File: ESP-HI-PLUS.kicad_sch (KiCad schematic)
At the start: 81 parts, among them J1 USB_C_Receptacle_USB2.0_14P, J2 0.71" LCD, J3 PR5L4015-5P-C-F, J4 PR5L4015-5P-C-F, Q1 AO3401A, Q2 NTK3139P, SW1 SKRPACE010, SW2 SKRPACE010, SW3 JS102011SAQN, U1 MAX40200AUK, U2 ESP32-S3-WROOM-1, U3 TLV75733PDBV, U4 TP4065, U5 DMM-4026-B-I2S-R, U6 MAX40200AUK, U7 MAX98357A, U8 LSM6DSV16X

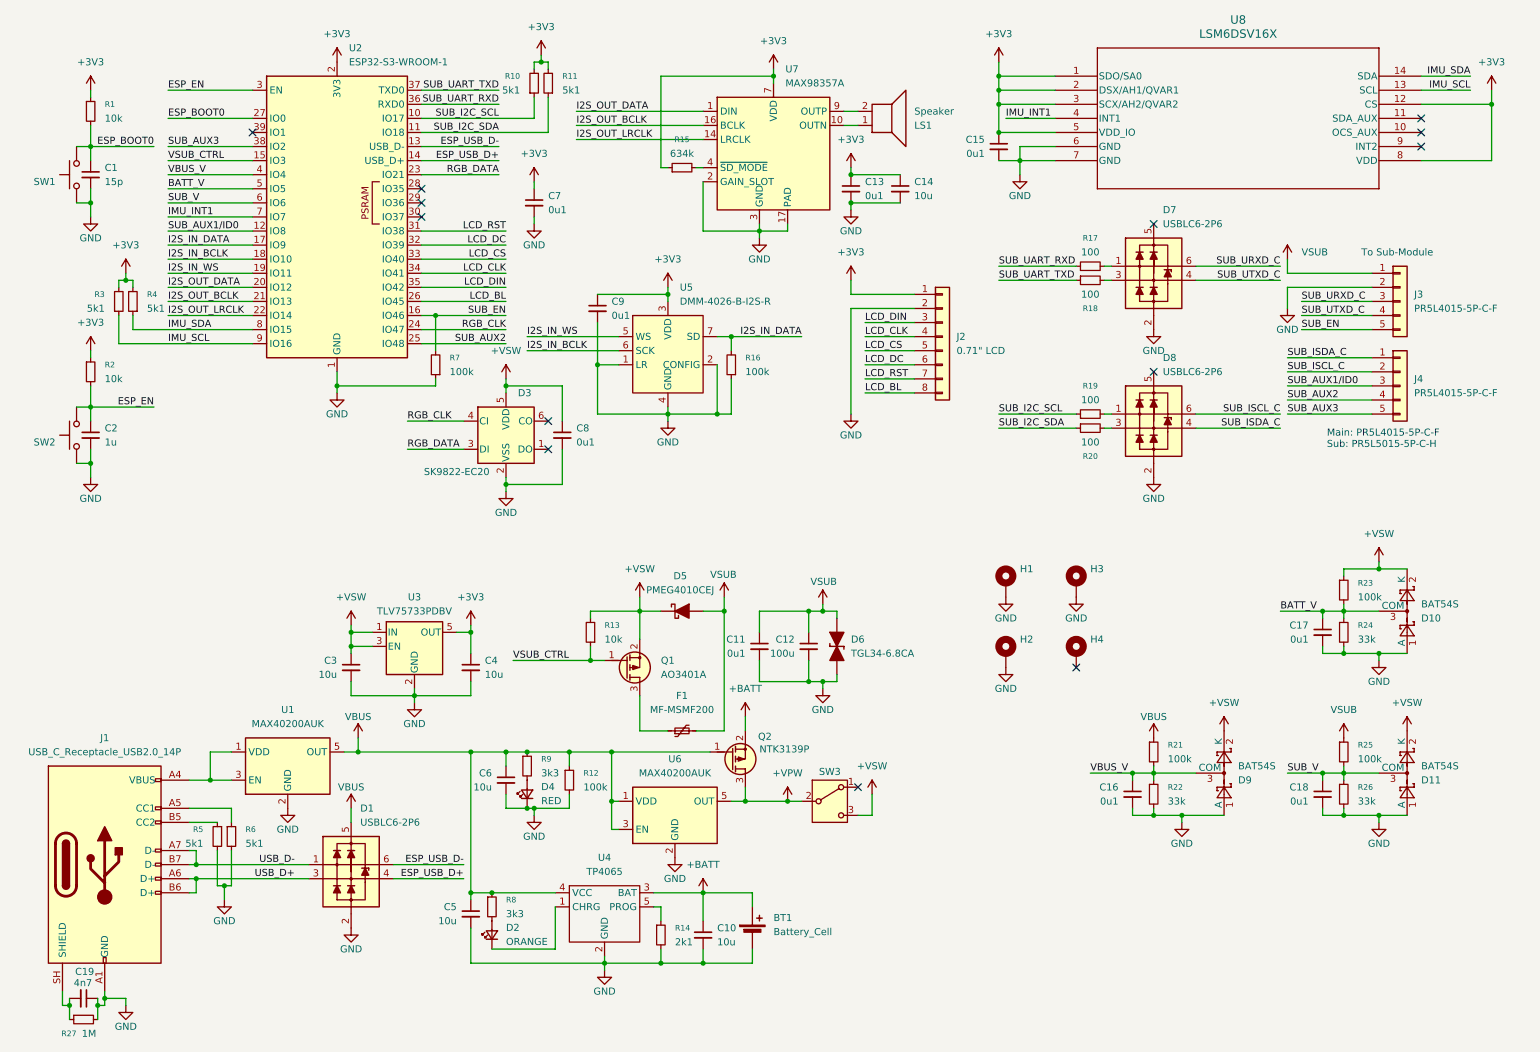
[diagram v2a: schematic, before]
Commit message: Added Sub-module Configuration Resistor and Resistor Table
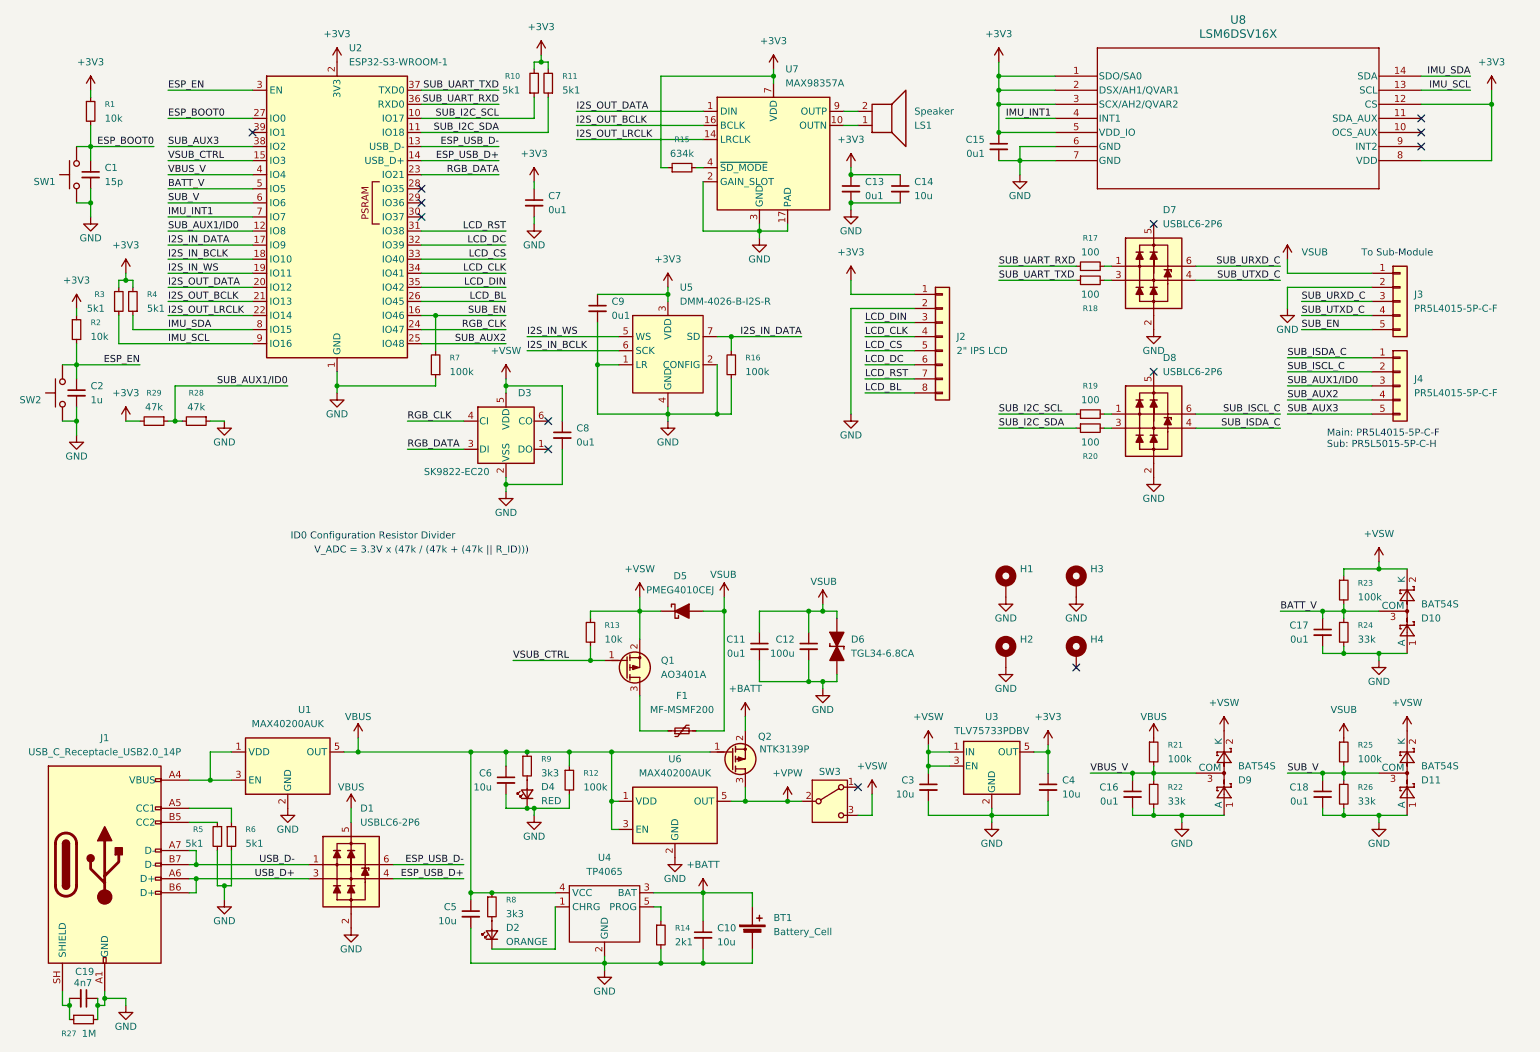
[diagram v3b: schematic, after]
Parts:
- added R28, R29: 47k, PCM_Resistor_SMD_AKL:R_0402_1005Metric, symbol Device:R_Small
- BT1, LS1: KiLib_Generator (none) -> connector/Molex
- C1, C10, C11, C12, C13, C14, C15, C16, C17, C18, C19, C2, C3, C4, C5, C6, C7, C8, C9, D2, F1: KiLib_Generator (none) -> SMD_2terminal_chip_molded
- D10, U6: KiLib_Generator (none) -> package/gullwing
- D11: footprint PCM_SparkFun-LED:APA102_2020-6Pin -> Package_TO_SOT_SMD:SOT-23; KiLib_Generator (none) -> package/gullwing
- D3: footprint LED_SMD:LED_0603_1608Metric -> PCM_SparkFun-LED:APA102_2020-6Pin
- D4: footprint PCM_Diode_SMD_AKL:D_SOD-323F -> LED_SMD:LED_0603_1608Metric; KiLib_Generator (none) -> SMD_2terminal_chip_molded
- D5: footprint Package_TO_SOT_SMD:SOT-23 -> PCM_Diode_SMD_AKL:D_SOD-323F
- D6: footprint PCM_Diode_SMD_AKL:D_SMA_TVS -> PCM_Diode_SMD_AKL:D_MiniMELF_TVS
- D7: footprint Package_TO_SOT_SMD:SOT-23 -> PCM_Package_TO_SOT_SMD_AKL:SOT-666
- D9: footprint PCM_Package_TO_SOT_SMD_AKL:SOT-666 -> Package_TO_SOT_SMD:SOT-23; KiLib_Generator (none) -> package/gullwing
- J1: footprint Connector_PinSocket_2.54mm:PinSocket_1x08_P2.54mm_Vertical -> Connector_USB:USB_C_Receptacle_HCTL_HC-TYPE-C-16P-01A
- J2: value 0.71" LCD -> 2" IPS LCD; footprint Connector_USB:USB_C_Receptacle_HCTL_HC-TYPE-C-16P-01A -> Connector_PinSocket_2.54mm:PinSocket_1x08_P2.54mm_Vertical; KiLib_Generator (none) -> connector/pin_header_socket
- J3, J4: KiLib_Generator (none) -> connector/pin_header_socket
- Q1: footprint PCM_Package_TO_SOT_SMD_AKL:SOT-723 -> PCM_Package_TO_SOT_SMD_AKL:SOT-23
- Q2: footprint PCM_Package_TO_SOT_SMD_AKL:SOT-23 -> PCM_Package_TO_SOT_SMD_AKL:SOT-723
- SW1: footprint Button_Switch_SMD:SW_SPDT_CK_JS102011SAQN -> Button_Switch_SMD:SW_Push_1P1T_NO_Vertical_Wuerth_434133025816
- SW3: footprint Button_Switch_SMD:SW_Push_1P1T_NO_Vertical_Wuerth_434133025816 -> Button_Switch_SMD:SW_SPDT_CK_JS102011SAQN
- U1: footprint RF_Module:ESP32-S3-WROOM-1 -> Package_TO_SOT_SMD:SOT-23-5; KiLib_Generator (none) -> package/gullwing
- U2: footprint MIC_DMM-4026-B-I2S-R:MIC_DMM-4026-B-I2S-R -> RF_Module:ESP32-S3-WROOM-1
- U3: footprint Package_DFN_QFN:TQFN-16-1EP_3x3mm_P0.5mm_EP1.23x1.23mm -> Package_TO_SOT_SMD:SOT-23-5; KiLib_Generator (none) -> package/gullwing
- U4: footprint LSM6DSV16X:LGA14_LSM6_STM -> PCM_Package_TO_SOT_SMD_AKL:SOT-23-5_BigPads
- U5: footprint Package_TO_SOT_SMD:SOT-23-5 -> MIC_DMM-4026-B-I2S-R:MIC_DMM-4026-B-I2S-R
- U7: footprint PCM_Package_TO_SOT_SMD_AKL:SOT-23-5_BigPads -> Package_DFN_QFN:TQFN-16-1EP_3x3mm_P0.5mm_EP1.23x1.23mm; KiLib_Generator (none) -> package/no_lead
- U8: footprint Package_TO_SOT_SMD:SOT-23-5 -> LSM6DSV16X:LGA14_LSM6_STM
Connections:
- net +3V3: now also R29.2
- net GND: now also R28.1
- net SUB_AUX1/ID0: now also R28.2, R29.1
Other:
- note added: "ID0 Configuration Resistor Divider"
- note added: "V_ADC = 3.3V x (47k / (47k + (47k || R_ID)))"
- title: (none) -> ESP-HI-PLUS
- moved on the sheet: C2, C3, C4, R2, SW2, U3

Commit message: ESP-HI-PLUS v1.1: added microSD card slot and combined I2S in/out ports
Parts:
- added J5: Micro_SD_Card, Connector_Card:microSD_HC_Hirose_DM3AT-SF-PEJM5, symbol Connector:Micro_SD_Card
- added R30, R31, R32, R33: 10k, PCM_Resistor_SMD_AKL:R_0402_1005Metric, symbol Device:R_Small
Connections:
- net +3V3: now also J5.4 (VDD), R30.2, R31.2, R32.2, R33.2
- net GND: now also J5.6 (VSS)
- net I2S_IN_BCLK: now also U7.16 (BCLK)
- net I2S_IN_DATA: now also U7.1 (DIN)
- net I2S_IN_WS: now also U7.14 (LRCLK)
- net SD_CS: now reaches U2.39 (IO1)
- net SD_CS: now also J5.2 (DAT3/CD), R30.1
- net I2S_OUT_BCLK renamed SD_SCLK
- net SD_SCLK: now also J5.5 (CLK), R33.1; no longer U7.16 (BCLK)
- net I2S_OUT_DATA renamed SD_MISO
- net SD_MISO: now also J5.7 (DAT0), R32.1; no longer U7.1 (DIN)
- net I2S_OUT_LRCLK renamed SD_MOSI
- net SD_MOSI: now also J5.3 (CMD), R31.1; no longer U7.14 (LRCLK)
- no-connect marks 13 -> 15
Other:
- moved on the sheet: H1, H2, H3, H4

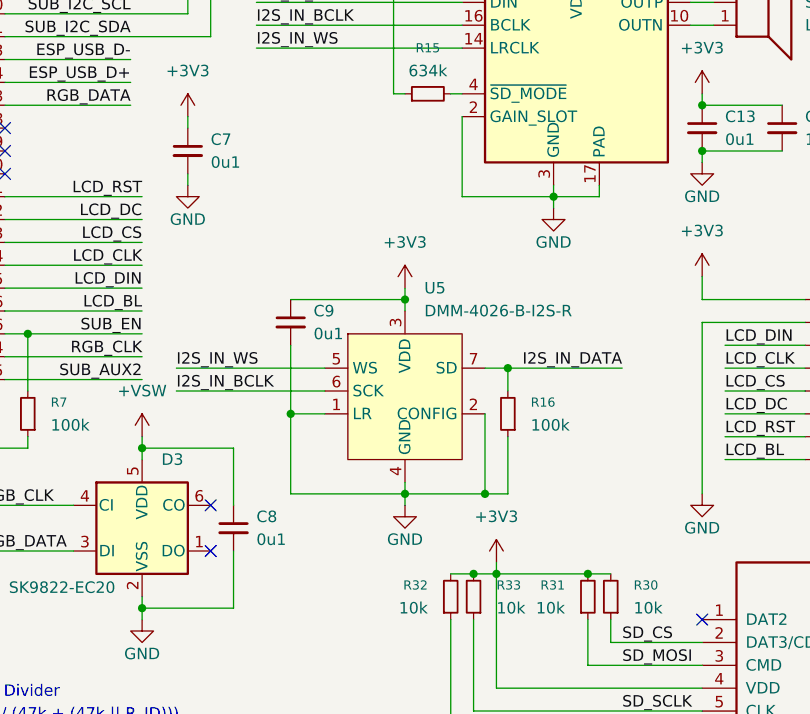
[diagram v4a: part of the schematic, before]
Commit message: ESP-HI-PLUS v1.15: changed size of 100u capacitor, changed microphone to ICS43434 for availability
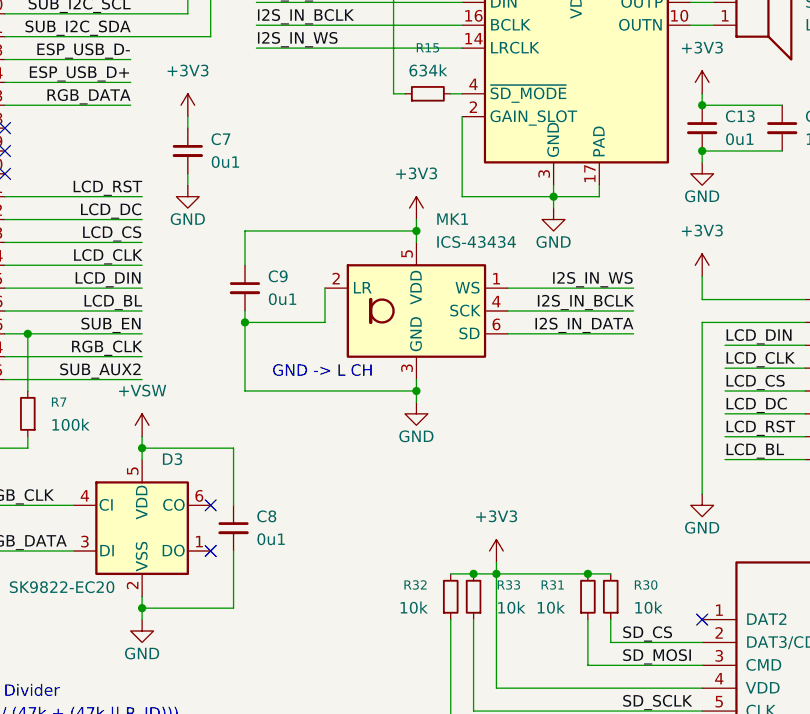
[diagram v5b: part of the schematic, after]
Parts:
- removed R16: 100k, PCM_Resistor_SMD_AKL:R_0402_1005Metric, symbol Device:R_Small
- removed U5: DMM-4026-B-I2S-R, MIC_DMM-4026-B-I2S-R:MIC_DMM-4026-B-I2S-R, symbol ESP-HI-PLUS Library:DMM-4026-B-I2S-R
- added MK1: ICS-43434, Sensor_Audio:InvenSense_ICS-43434-6_3.5x2.65mm, symbol Sensor_Audio:ICS-43434
- C12: footprint Capacitor_SMD:C_0402_1005Metric -> Capacitor_SMD:C_0805_2012Metric
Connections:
- net +3V3: now also MK1.5 (VDD)
- net GND: now also MK1.2 (LR), MK1.3 (GND)
- net I2S_IN_BCLK: now also MK1.4 (SCK)
- net I2S_IN_DATA: now also MK1.6 (SD)
- net I2S_IN_WS: now also MK1.1 (WS)
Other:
- note added: "GND -> L CH"
- moved on the sheet: C9

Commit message: ESP-HI-PLUS v1.15.1: changed VSUB ESD diode
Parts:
- D6: value TGL34-6.8CA -> SMF6.8CA; footprint PCM_Diode_SMD_AKL:D_MiniMELF_TVS -> PCM_Diode_SMD_AKL:D_SOD-123F
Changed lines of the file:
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@@
 			)
 		)
-		(property "Value" "TGL34-6.8CA"
+		(property "Value" "SMF6.8CA"
 			(at 162.56 128.2699 90)
 			(show_name no)
@@
 			)
 		)
-		(property "Footprint" "PCM_Diode_SMD_AKL:D_MiniMELF_TVS"
+		(property "Footprint" "PCM_Diode_SMD_AKL:D_SOD-123F"
 			(at 160.02 127 0)
 			(hide yes)

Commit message: Setup STM32U5 pinout for Portable submodule
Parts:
- removed U4: TP4065, PCM_Package_TO_SOT_SMD_AKL:SOT-23-5_BigPads, symbol ESP-HI-PLUS Library:TP4065
- added U5: TP4065, Package_TO_SOT_SMD:SOT-23-5_HandSoldering, symbol ESP-HI-PLUS Library:TP4065
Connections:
- net +BATT: now also U5.3 (BAT)
- net GND: now also U5.2 (GND)
- net VBUS: now also U5.4 (VCC)
- net at D2.1 (K): now also U5.1 (CHRG)
- net at R14.1: now also U5.5 (PROG)
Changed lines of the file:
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@@
 	)
 	(symbol
-		(lib_id "ESP-HI-PLUS Library:TP4065")
-		(at 118.11 173.99 0)
-		(unit 1)
-		(body_style 1)
-		(exclude_from_sim no)
-		(in_bom yes)
-		(on_board yes)
-		(in_pos_files yes)
-		(dnp no)
-		(property "Reference" "U4"
-			(at 118.11 165.1 0)
-			(show_name no)
-			(do_not_autoplace no)
-			(effects
-				(font
-					(size 1.27 1.27)
-				)
-			)
-		)
-		(property "Value" "TP4065"
-			(at 118.11 167.64 0)
-			(show_name no)
-			(do_not_autoplace no)
-			(effects
-				(font
-					(size 1.27 1.27)
-				)
-			)
-		)
-		(property "Footprint" "PCM_Package_TO_SOT_SMD_AKL:SOT-23-5_BigPads"
-			(at 118.11 153.416 0)
-			(hide yes)
-			(show_name no)
-			(do_not_autoplace no)
-			(effects
-				(font
-					(size 1.27 1.27)
-				)
-			)
-		)
-		(property "Datasheet" "http://tp-asic.com/res/tp-asic/pdres/202302/TP4065.pdf"
-			(at 116.332 151.892 0)
-			(hide yes)
-			(show_name no)
-			(do_not_autoplace no)
-			(effects
-				(font
-					(size 1.27 1.27)
-				)
-			)
-		)
-		(property "Description" ""
-			(at 118.11 173.99 0)
-			(hide yes)
-			(show_name no)
-			(do_not_autoplace no)
-			(effects
-				(font
-					(size 1.27 1.27)
-				)
-			)
-		)
-		(pin "2"
-		)
-		(pin "1"
-		)
-		(pin "3"
-		)
-		(pin "4"
-		)
-		(pin "5"
-		)
-		(instances
-			(project "ESP-HI-PLUS"
-				(path "/38bc51f5-c7e2-4cb9-a161-d419c07b2cad"
-					(reference "U4")
-					(unit 1)
-				)
-			)
-		)
-	)
-	(symbol
 		(lib_id "Device:R_Small")
 		(at 22.86 69.85 0)
@@
 					(unit 1)
 				)
+			)
+		)
+	)
+	(symbol
+		(lib_name "TP4065_1")
+		(lib_id "ESP-HI-PLUS Library:TP4065")
+		(at 118.11 175.26 0)
+		(unit 1)
+		(body_style 1)
+		(exclude_from_sim no)
+		(in_bom yes)
+		(on_board yes)
+		(in_pos_files yes)
+		(dnp no)
+		(fields_autoplaced yes)
+		(property "Reference" "U5"
+			(at 118.11 165.1 0)
+			(show_name no)
+			(do_not_autoplace no)
+			(effects
+				(font
+					(size 1.27 1.27)
+				)
+			)
+		)
+		(property "Value" "TP4065"
+			(at 118.11 167.64 0)
+			(show_name no)
+			(do_not_autoplace no)
+			(effects
+				(font
+					(size 1.27 1.27)
+				)
+			)
+		)
+		(property "Footprint" "Package_TO_SOT_SMD:SOT-23-5_HandSoldering"
+			(at 118.364 154.94 0)
+			(hide yes)
+			(show_name no)
+			(do_not_autoplace no)
+			(effects
+				(font
+					(size 1.27 1.27)
+				)
+			)
+		)
+		(property "Datasheet" ""
+			(at 118.11 175.26 0)
+			(hide yes)
+			(show_name no)
+			(do_not_autoplace no)
+			(effects
+				(font
+					(size 1.27 1.27)
+				)
+			)
+		)
+		(property "Description" ""
+			(at 118.11 175.26 0)
+			(hide yes)
+			(show_name no)
+			(do_not_autoplace no)
+			(effects
+				(font
+					(size 1.27 1.27)
+				)
+			)
+		)
+		(pin "1"
+		)
+		(pin "3"
+		)
+		(pin "4"
+		)
+		(pin "5"
+		)
+		(pin "2"
+		)
+		(instances
+			(project "ESP-HI-PLUS"
+				(path "/38bc51f5-c7e2-4cb9-a161-d419c07b2cad"
+					(reference "U5")
+					(unit 1)
+				)
